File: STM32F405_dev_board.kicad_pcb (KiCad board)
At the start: 4 copper layers, 39.4 x 83.8 mm, 46 parts, among them IC2 FT232RNL-REEL, J1 Conn_ARM_JTAG_SWD_20, J2 Conn_01x20_Pin, J3 Conn_01x20_Pin, J6 USB4800-03-A, U1 STM32F405RGT6, Y1 8MHz, Y2 Crystal_GND23

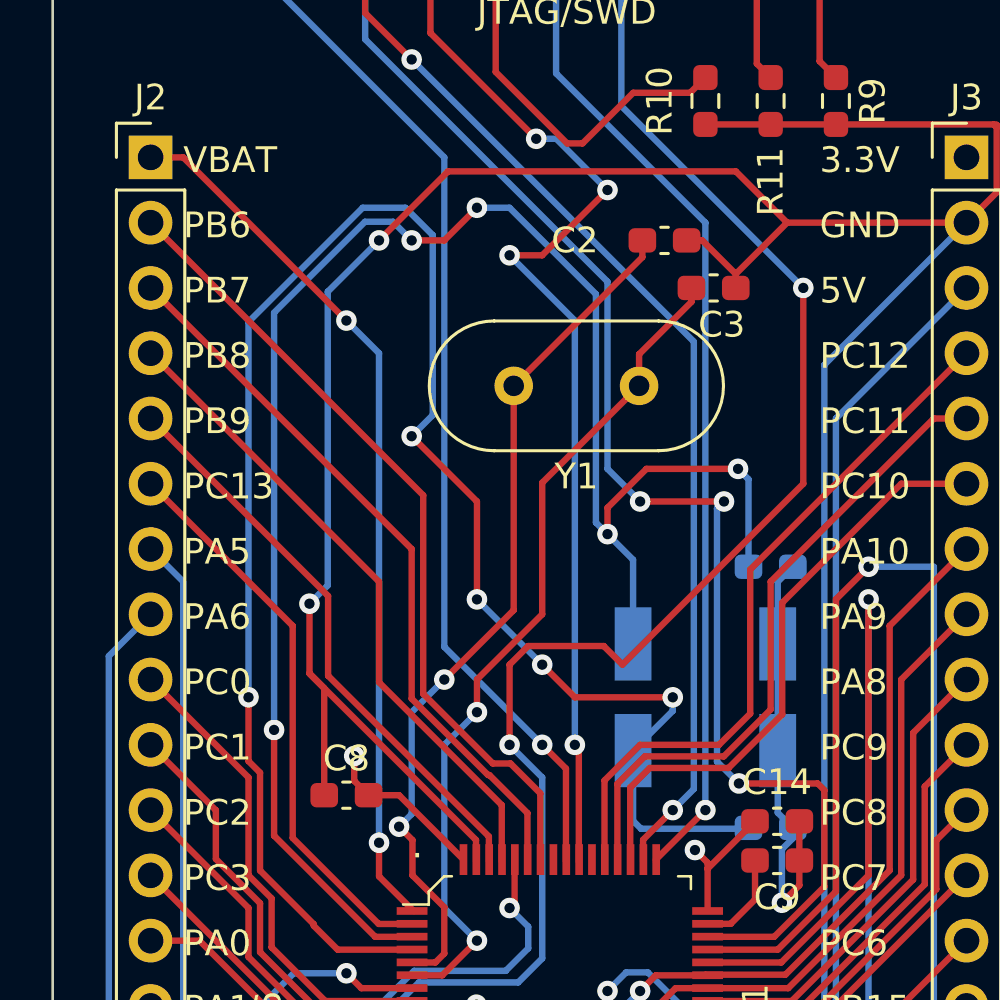
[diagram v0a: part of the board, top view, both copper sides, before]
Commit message: Changed 8MHz oscillator to SMD one
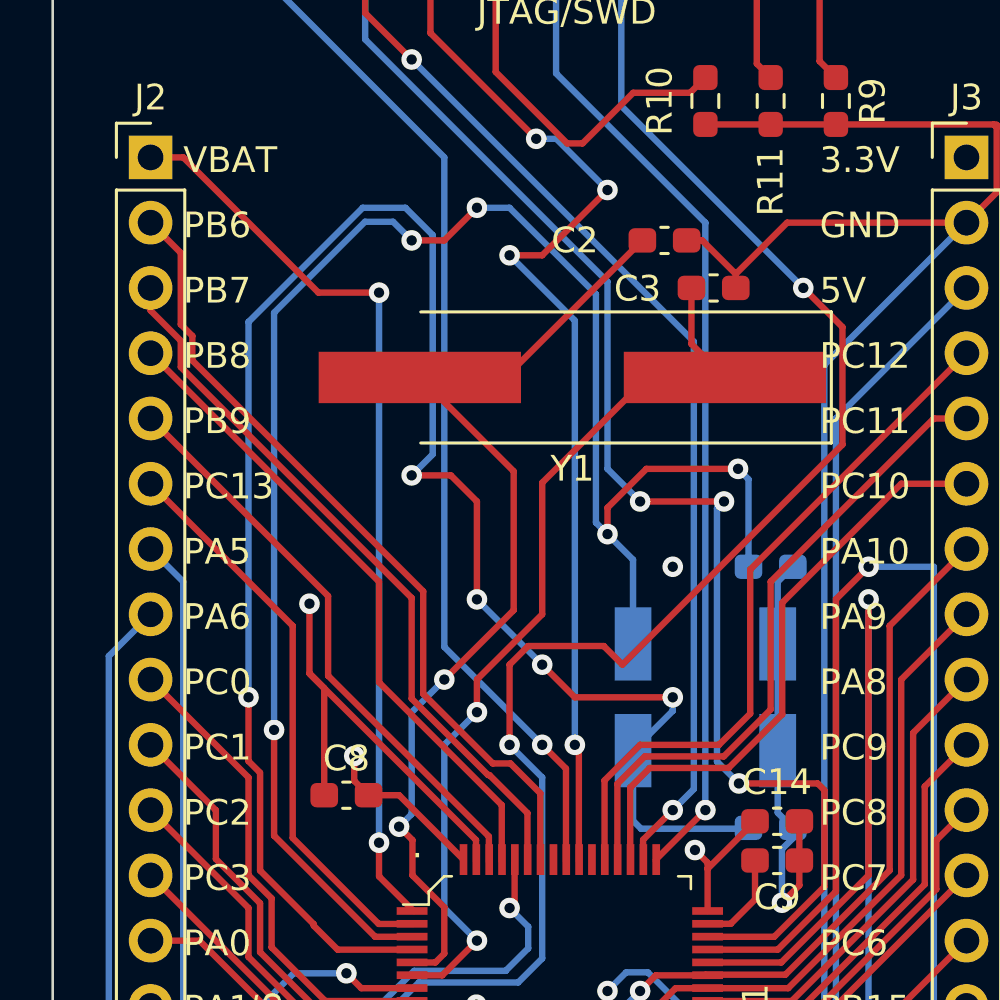
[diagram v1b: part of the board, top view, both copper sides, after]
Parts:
- Y1: footprint Crystal:Crystal_HC49-4H_Vertical -> Crystal:Crystal_SMD_HC49-SD_HandSoldering
- moved Y1 2.62 mm to (146.0, 89.2)
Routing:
- net GND: track 246.1 -> 213.0 mm
- net OSC_IN: track 33.7 -> 38.7 mm
- net OSC_OUT: track 32.9 -> 35.8 mm
- net VBAT: track 34.3 -> 35.7 mm
- net RESET: track 137.6 -> 138.9 mm
- net OSC32_OUT: track 73.1 -> 74.0 mm

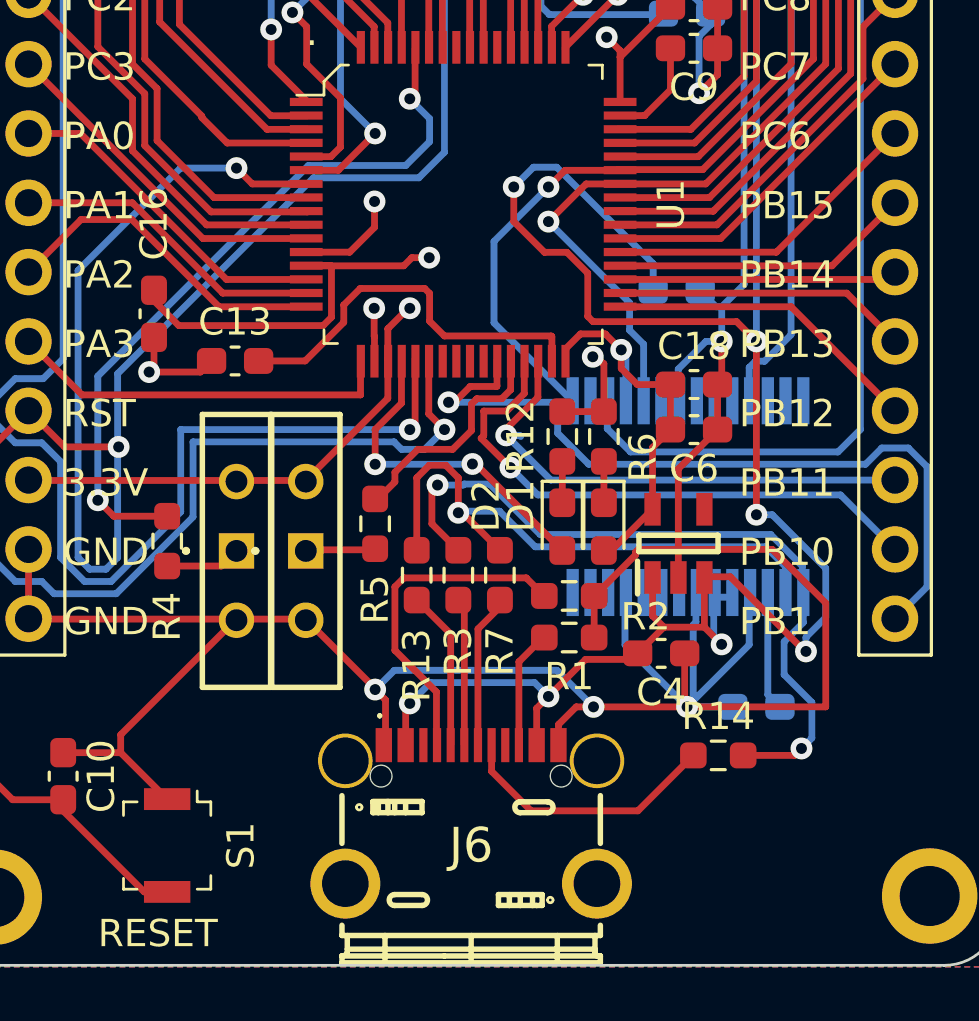
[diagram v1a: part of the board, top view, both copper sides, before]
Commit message: Fixed FT232RL connection
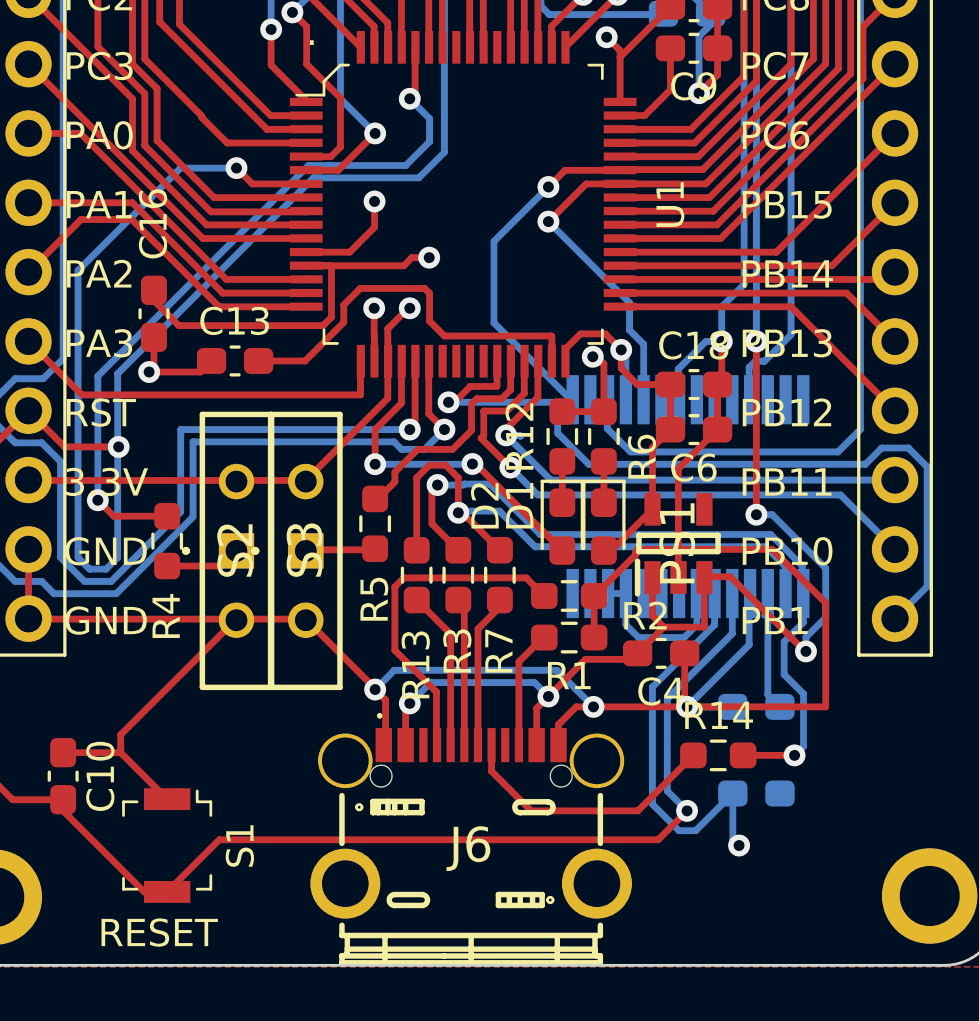
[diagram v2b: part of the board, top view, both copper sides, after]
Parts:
- moved C1 18.6 mm to (156.2, 135.3)
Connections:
- C1 pad 2: 5V -> VCC3V3
- IC2 pad 19: 5V -> RESET
- IC2 pad 20: 5V -> VCC3V3
- IC2 pad 26: unconnected-(IC2-TEST-Pad26) -> GND
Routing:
- net RESET: track 138.9 -> 168.4 mm, vias 4 -> 5
- net 5V: track 97.2 -> 72.8 mm, vias 7 -> 5
- net VCC3V3: track 59.4 -> 74.0 mm, vias 5 -> 6
- net GND: track 213.0 -> 209.1 mm
